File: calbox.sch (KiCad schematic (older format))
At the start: 2 parts, among them X1 ACHL_XO

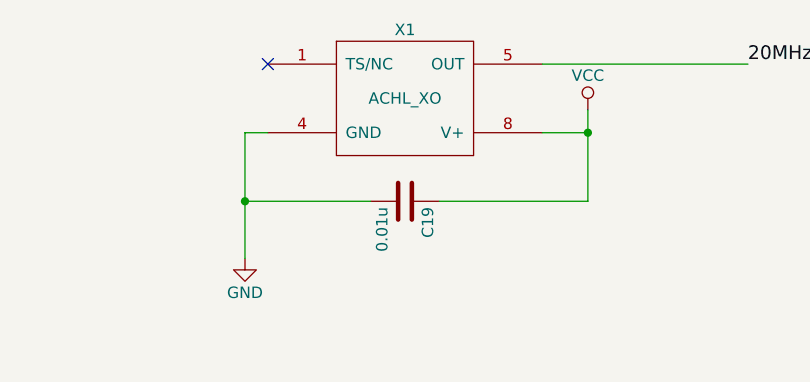
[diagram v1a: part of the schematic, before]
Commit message: R2 PCB rotary switches closer to middle of board
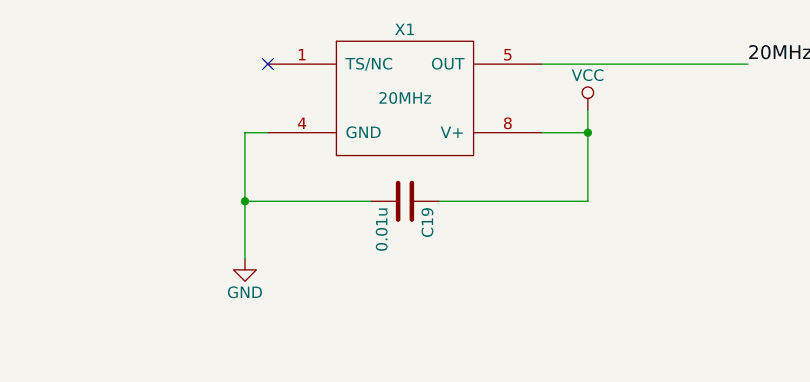
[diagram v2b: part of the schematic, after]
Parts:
- X1: value ACHL_XO -> 20MHz; Distributor (none) -> Mouser; Distributor PN (none) -> 815-ACHL-20-EK; Manufacturer (none) -> ABRACON; Manufacturer PN (none) -> ACHL-20.000MHZ-EK; URL (none) -> http://www.mouser.com/Search/ProductDetail.aspx?R=ACHL-20.0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; Unit Price (none) -> 1.76
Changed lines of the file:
@@
 encoding utf-8
 Sheet 1 6
-Title ""
+Title "calbox"
 Date ""
 Rev ""
@@
 NoConn ~ 2200 1200
 $Comp
-L GND #PWR1
+L GND #PWR01
 U 1 1 58C89F83
 P 2100 2050
-F 0 "#PWR1" H 2100 1800 50  0001 C CNN
+F 0 "#PWR01" H 2100 1800 50  0001 C CNN
 F 1 "GND" H 2100 1900 50  0000 C CNN
 F 2 "" H 2100 2050 50  0000 C CNN
@@
 	2100 1500 2200 1500
 $Comp
-L VCC #PWR2
+L VCC #PWR02
 U 1 1 58C89FEC
 P 3600 1400
-F 0 "#PWR2" H 3600 1250 50  0001 C CNN
+F 0 "#PWR02" H 3600 1250 50  0001 C CNN
 F 1 "VCC" H 3600 1550 50  0000 C CNN
 F 2 "" H 3600 1400 50  0000 C CNN
@@
 P 2800 1350
 F 0 "X1" H 2800 1650 50  0000 C CNN
-F 1 "ACHL_XO" H 2800 1350 50  0000 C CNN
+F 1 "20MHz" H 2800 1350 50  0000 C CNN
 F 2 "Oscillators:OSC_DIP8" H 2800 1350 50  0001 C CNN
-F 3 "" H 2800 1350 50  0000 C CNN
+F 3 "http://www.mouser.com/ds/2/3/ACHL-24088.pdf" H 2800 1350 50  0001 C CNN
+F 4 "ABRACON" H 2800 1350 60  0001 C CNN "Manufacturer"
+F 5 "ACHL-20.000MHZ-EK" H 2800 1350 60  0001 C CNN "Manufacturer PN"
+F 6 "Mouser" H 2800 1350 60  0001 C CNN "Distributor"
+F 7 "815-ACHL-20-EK" H 2800 1350 60  0001 C CNN "Distributor PN"
+F 8 "http://www.mouser.com/Search/ProductDetail.aspx?R=ACHL-20.000MHZ-EKvirtualkey52750000virtualkey815-ACHL-20-EK" H 2800 1350 60  0001 C CNN "URL"
+F 9 "1.76" H 2800 1350 60  0001 C CNN "Unit Price"
 	1    2800 1350
 	1    0    0    -1
